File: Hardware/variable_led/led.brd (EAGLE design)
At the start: 160 x 100 mm, 12 parts

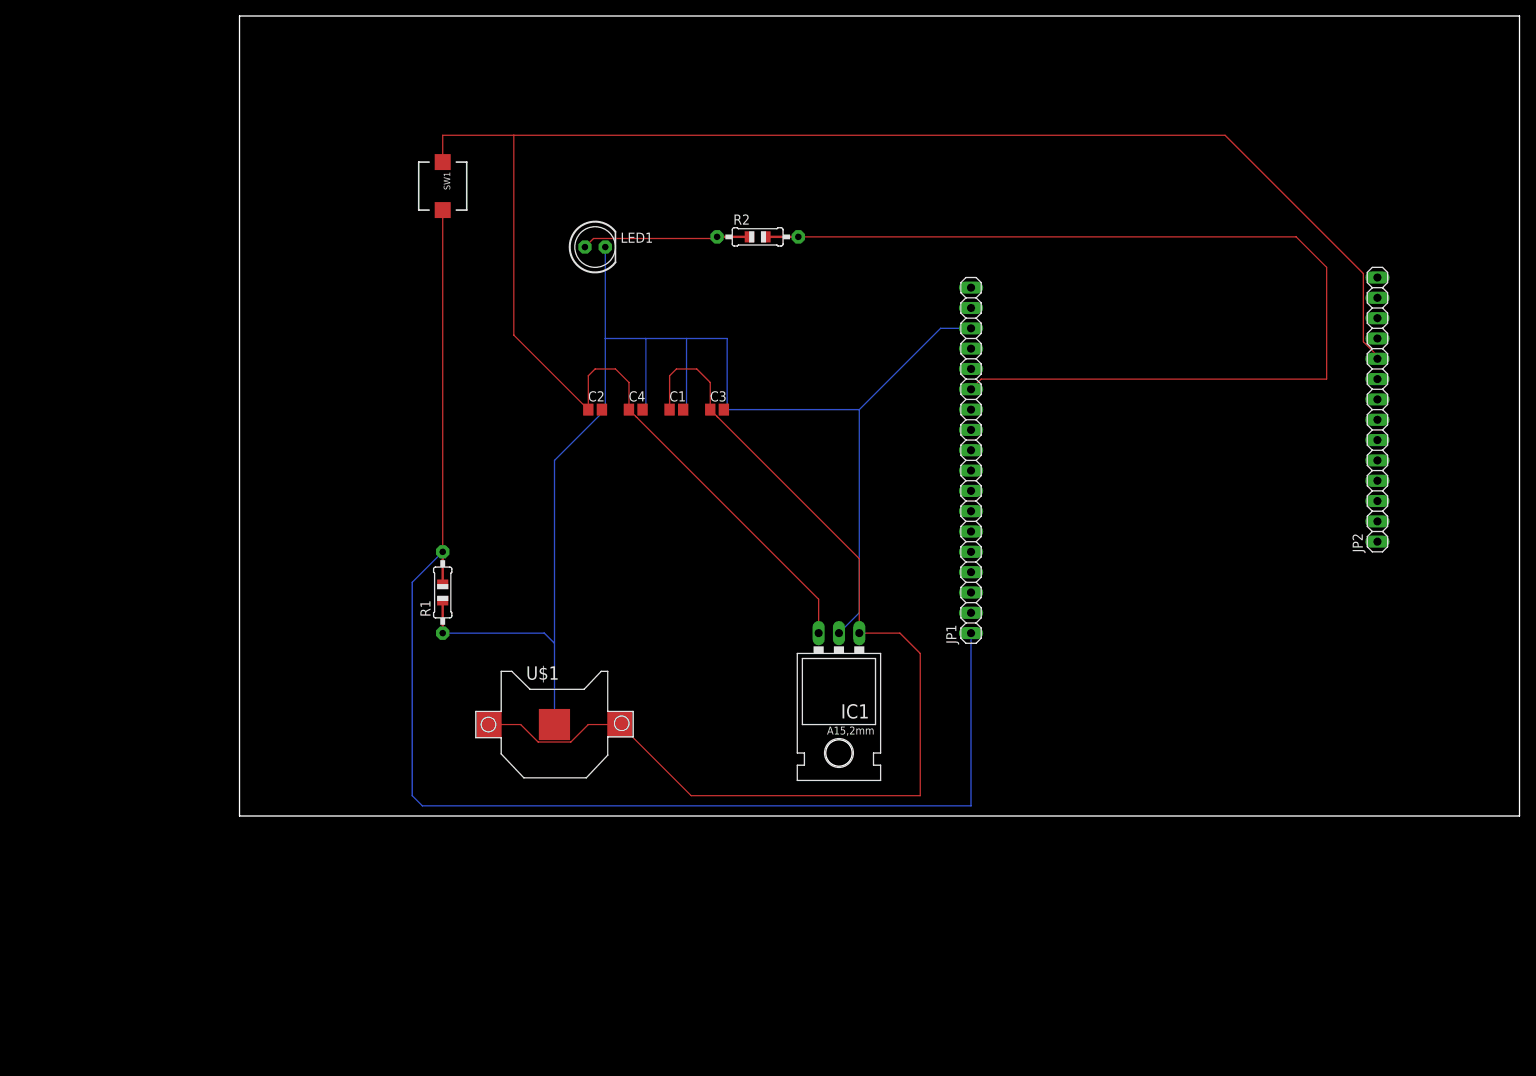
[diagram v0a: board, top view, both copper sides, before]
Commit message: Updated schematics without the voltage regulator
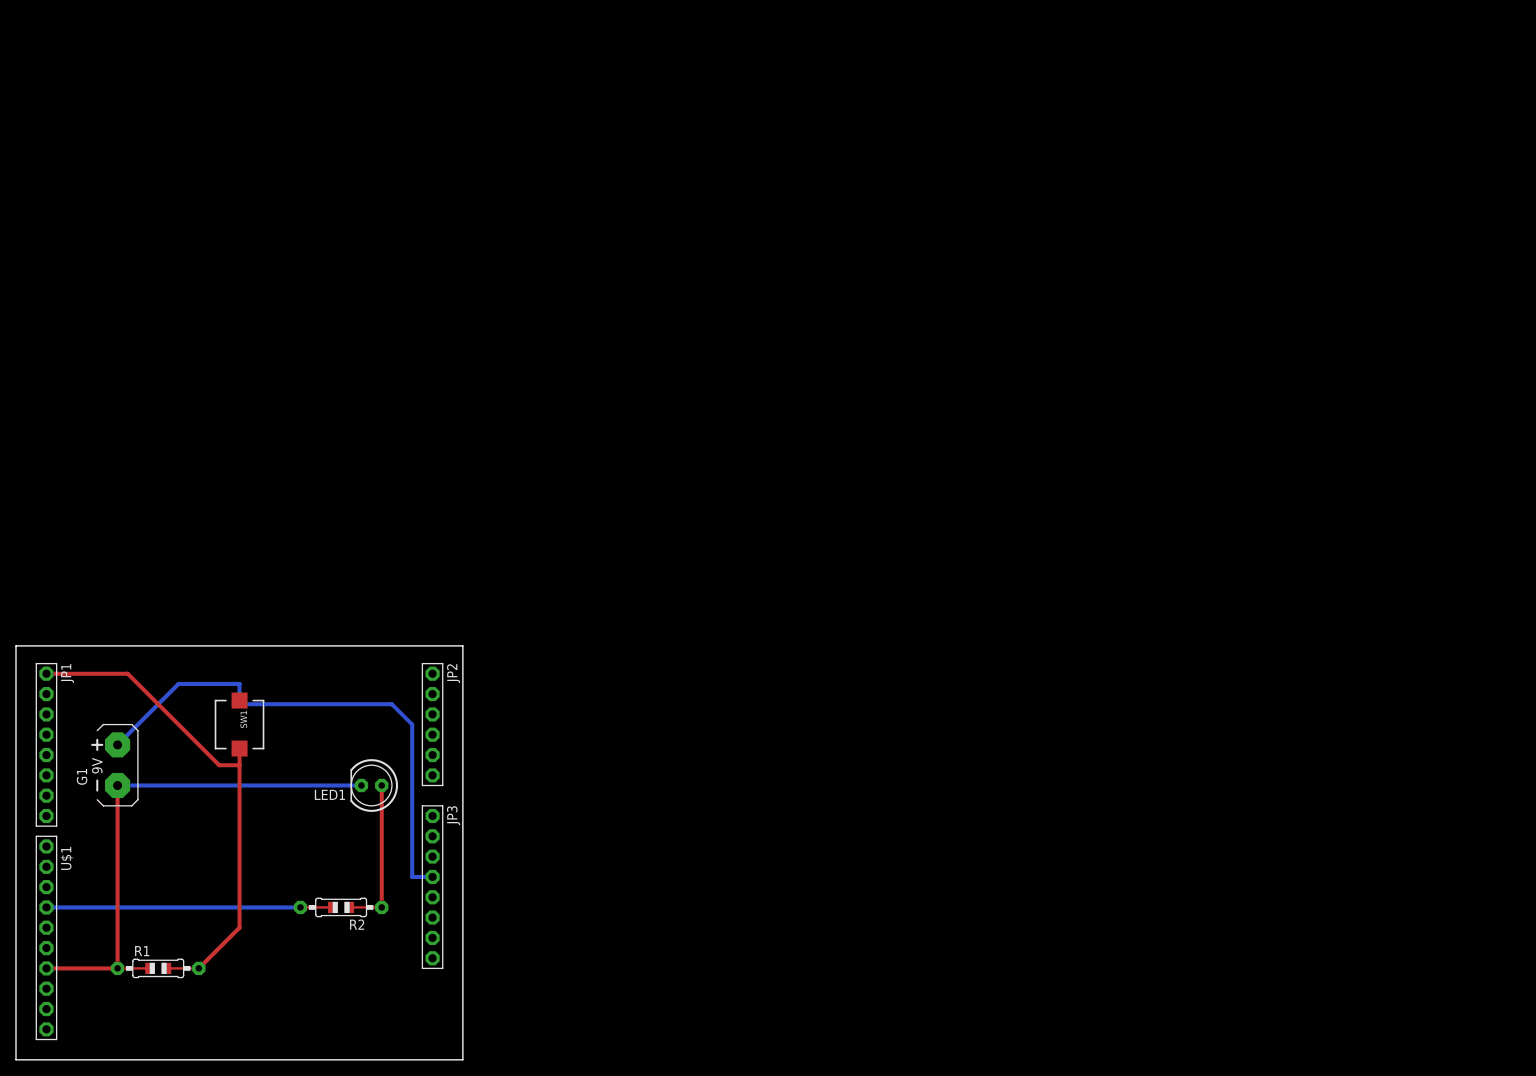
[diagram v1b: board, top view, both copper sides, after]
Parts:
- removed C1, C2: 10u, adafruit:C0805
- removed C3, C4: 0.1u, adafruit:C0805
- removed IC1: (no value), v-reg:78XXL
- added G1: AB9V, battery:AB9V
- added JP3: (no value), adafruit:1X08-BIG
- JP1: device adafruit:1X18 -> adafruit:1X08-BIG
- JP2: device adafruit:1X14 -> adafruit:1X06-BIG
- U$1: value 9V -> PINHD-1X10; device adafruit:CR1220-SMD -> adafruit:1X10-BIG
- moved JP2 124.5 mm to (24.1, 11.4), turned to 270 degrees
- moved JP1 120.9 mm to (-24.1, 8.89), turned to 270 degrees
- moved R2 98.7 mm to (12.7, -11.4), turned to 180 degrees
- moved LED1 72.9 mm to (16.5, 3.81), turned to 180 degrees
- moved SW1 71.9 mm to (0.00, 11.4)
- moved U$1 68.9 mm to (-24.1, -15.2), turned to 270 degrees
- moved R1 58.9 mm to (-10.2, -19.1), turned to 0 degrees
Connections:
- removed net V+: C1.1, C3.1, IC1.IN, U$1.+$1, U$1.+$2
- net 5V: now also G1.+, JP3.4; no longer C2.1, C4.1, IC1.OUT, JP2.10
- net GND: now also G1.-, U$1.7; no longer C1.2, C2.2, C3.2, C4.2, IC1.GND, JP1.16, U$1.-
- net N$2: now also U$1.4; no longer JP1.13
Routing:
- net 5V: track 228.3 -> 65.2 mm
- net V+: track 136.7 -> 0.00 mm
- net GND: track 182.4 -> 62.2 mm
- net N$4: track 166.9 -> 58.4 mm
- net N$2: track 126.6 -> 31.8 mm
- net N$3: track 17.0 -> 15.2 mm
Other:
- board size 160 x 100 mm -> 55.9 x 51.7 mm

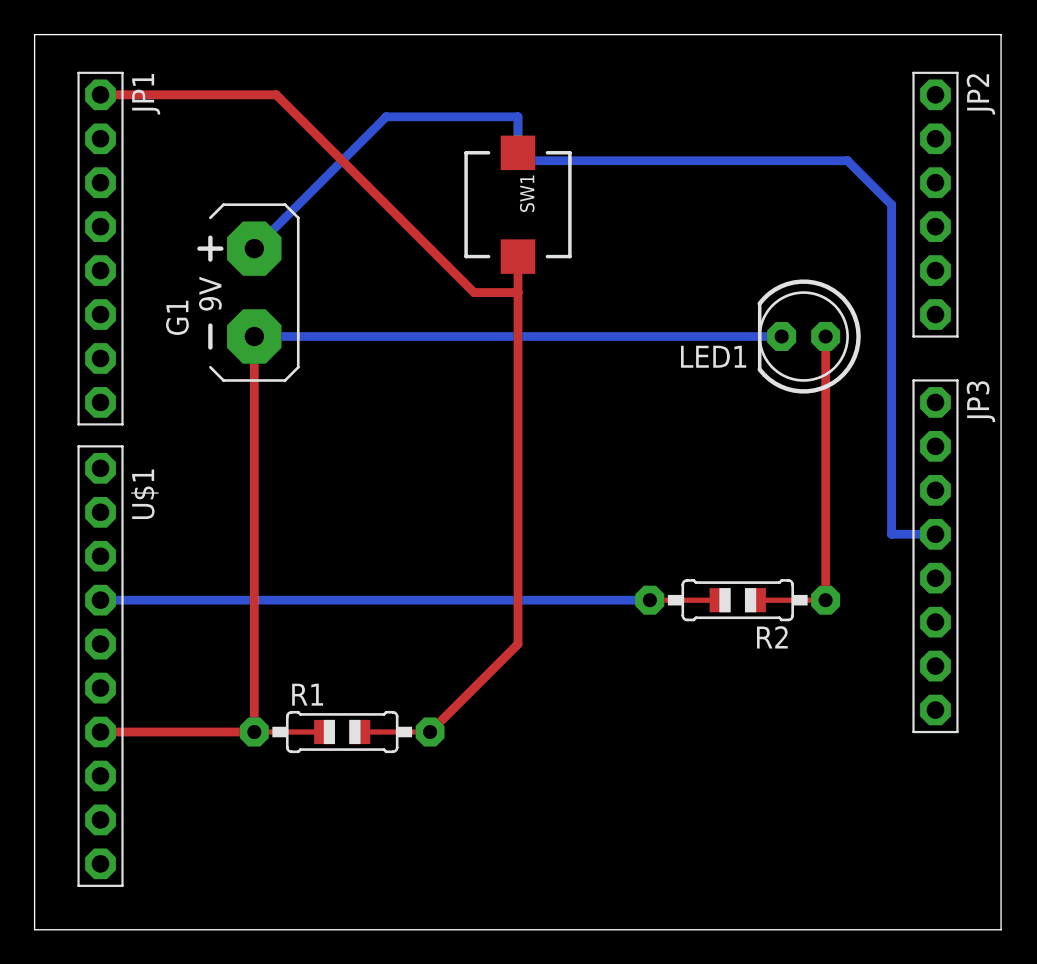
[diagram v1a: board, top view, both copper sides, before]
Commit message: Changed LED to two pins and changed board to single side
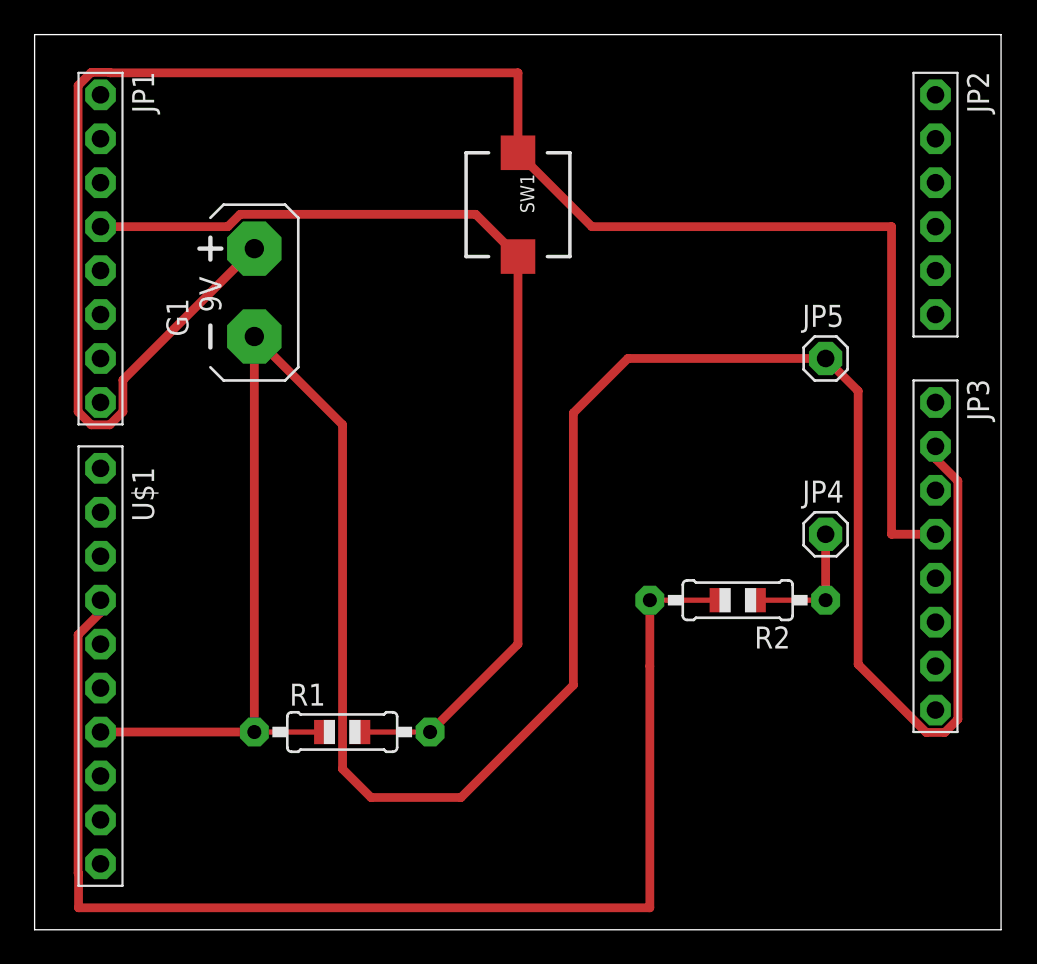
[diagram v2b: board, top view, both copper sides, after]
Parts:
- removed LED1: (no value), adafruit:LED5MM
- added JP4, JP5: (no value), adafruit:1X01
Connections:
- net GND: now also JP3.2, JP5.1; no longer LED1.K
- net N$3: now also JP4.1; no longer LED1.A
- net N$4: now also JP1.4; no longer JP1.1
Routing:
- net GND: track 62.2 -> 149.7 mm
- net 5V: track 65.2 -> 108.7 mm
- net N$2: track 31.8 -> 69.1 mm
- net N$3: track 15.2 -> 3.81 mm
- net N$4: track 58.4 -> 55.0 mm
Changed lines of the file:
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@@
 <dimension x1="24.13" y1="5.08" x2="24.13" y2="0" x3="29.21" y3="2.54" textsize="1.778" layer="1" unit="inch"/>
 <dimension x1="-24.13" y1="17.78" x2="24.13" y2="17.78" x3="0" y3="27.94" textsize="1.778" layer="1" unit="inch"/>
+<dimension x1="-27.94" y1="21.26" x2="27.92" y2="21.26" x3="-0.01" y3="31.75" textsize="1.778" layer="1" unit="inch"/>
+<dimension x1="-27.94" y1="21.26" x2="-27.94" y2="-30.48" x3="-36.83" y3="-4.61" textsize="1.778" layer="1" unit="inch"/>
 </plain>
 <attributes>
@@
 </autorouter>
 <elements>
-<element name="LED1" library="adafruit" library_urn="urn:adsk.eagle:library:420" package="LED5MM" package3d_urn="urn:adsk.eagle:package:6240538/1" value="" x="16.51" y="3.81" rot="R180">
-<attribute name="NAME" x="13.335" y="3.2766" size="1.27" layer="25" ratio="10" rot="R180"/>
-<attribute name="VALUE" x="13.3096" y="5.6134" size="1.27" layer="27" ratio="10" rot="R180"/>
-</element>
 <element name="R1" library="adafruit" library_urn="urn:adsk.eagle:library:420" package="0805-THM" package3d_urn="urn:adsk.eagle:package:6240726/1" value="100k" x="-10.16" y="-19.05">
 <attribute name="NAME" x="-13.208" y="-17.526" size="1.27" layer="25" ratio="10"/>
@@
 <attribute name="VALUE" x="20.955" y="1.27" size="1.27" layer="27" rot="R270"/>
 </element>
+<element name="JP4" library="adafruit" library_urn="urn:adsk.eagle:library:420" package="1X01" package3d_urn="urn:adsk.eagle:package:6240654/1" value="" x="17.78" y="-7.62">
+<attribute name="NAME" x="16.4338" y="-5.7912" size="1.27" layer="25" ratio="10"/>
+<attribute name="VALUE" x="16.51" y="-10.795" size="1.27" layer="27"/>
+</element>
+<element name="JP5" library="adafruit" library_urn="urn:adsk.eagle:library:420" package="1X01" package3d_urn="urn:adsk.eagle:package:6240654/1" value="" x="17.78" y="2.54">
+<attribute name="NAME" x="16.4338" y="4.3688" size="1.27" layer="25" ratio="10"/>
+<attribute name="VALUE" x="16.51" y="-0.635" size="1.27" layer="27"/>
+</element>
 </elements>
 <signals>
 <signal name="GND">
-<contactref element="LED1" pad="K"/>
 <contactref element="R1" pad="1"/>
 <contactref element="G1" pad="-"/>
@@
 <wire x1="-15.24" y1="3.81" x2="-15.24" y2="-19.05" width="0.508" layer="1"/>
 <wire x1="-15.24" y1="-19.05" x2="-24.13" y2="-19.05" width="0.508" layer="1"/>
-<wire x1="15.24" y1="3.81" x2="-15.24" y2="3.81" width="0.508" layer="16"/>
+<wire x1="-15.24" y1="3.81" x2="-10.141" y2="-1.289" width="0.508" layer="1"/>
+<wire x1="-10.141" y1="-1.289" x2="-10.141" y2="-21.1883375" width="0.508" layer="1"/>
+<wire x1="-8.4947375" y1="-22.8346" x2="-10.141" y2="-21.1883375" width="0.508" layer="1"/>
+<wire x1="-3.29446875" y1="-22.8346" x2="-8.4947375" y2="-22.8346" width="0.508" layer="1"/>
+<wire x1="3.2004" y1="-16.33973125" x2="-3.29446875" y2="-22.8346" width="0.508" layer="1"/>
+<contactref element="JP3" pad="2"/>
+<wire x1="23.593425" y1="-19.0754" x2="24.666575" y2="-19.0754" width="0.508" layer="1"/>
+<wire x1="24.666575" y1="-19.0754" x2="25.4254" y2="-18.316575" width="0.508" layer="1"/>
+<wire x1="25.4254" y1="-18.316575" x2="25.4254" y2="-4.543425" width="0.508" layer="1"/>
+<wire x1="19.6596" y1="-15.141575" x2="23.593425" y2="-19.0754" width="0.508" layer="1"/>
+<wire x1="24.13" y1="-3.248025" x2="24.13" y2="-2.54" width="0.508" layer="1"/>
+<wire x1="25.4254" y1="-4.543425" x2="24.13" y2="-3.248025" width="0.508" layer="1"/>
+<contactref element="JP5" pad="1"/>
+<wire x1="17.78" y1="2.54" x2="6.35" y2="2.54" width="0.508" layer="1"/>
+<wire x1="6.35" y1="2.54" x2="3.2004" y2="-0.6096" width="0.508" layer="1"/>
+<wire x1="3.2004" y1="-0.6096" x2="3.2004" y2="-16.33973125" width="0.508" layer="1"/>
+<wire x1="19.6596" y1="0.6604" x2="17.78" y2="2.54" width="0.508" layer="1"/>
+<wire x1="19.6596" y1="0.6604" x2="19.6596" y2="-15.141575" width="0.508" layer="1"/>
 </signal>
 <signal name="N$2">
 <contactref element="R2" pad="2"/>
 <contactref element="U$1" pad="4"/>
-<wire x1="7.62" y1="-11.43" x2="-24.13" y2="-11.43" width="0.508" layer="16"/>
+<wire x1="-24.13" y1="-11.43" x2="-24.13" y2="-12.138025" width="0.508" layer="1"/>
+<wire x1="-25.4254" y1="-27.206575" x2="-25.4" y2="-27.231975" width="0.508" layer="1"/>
+<wire x1="-25.4" y1="-27.231975" x2="-25.4" y2="-29.21" width="0.508" layer="1"/>
+<wire x1="-24.13" y1="-12.138025" x2="-25.4254" y2="-13.433425" width="0.508" layer="1"/>
+<wire x1="-25.4254" y1="-13.433425" x2="-25.4254" y2="-27.206575" width="0.508" layer="1"/>
+<wire x1="7.62" y1="-29.21" x2="-25.4" y2="-29.21" width="0.508" layer="1"/>
+<wire x1="7.62" y1="-11.43" x2="7.62" y2="-15.24" width="0.508" layer="1"/>
+<wire x1="7.62" y1="-15.24" x2="7.62" y2="-29.21" width="0.508" layer="1"/>
 </signal>
 <signal name="N$3">
 <contactref element="R2" pad="1"/>
-<contactref element="LED1" pad="A"/>
-<wire x1="17.78" y1="3.81" x2="17.78" y2="-11.43" width="0.508" layer="1"/>
+<contactref element="JP4" pad="1"/>
+<wire x1="17.78" y1="-7.62" x2="17.78" y2="-11.43" width="0.508" layer="1"/>
 </signal>
 <signal name="N$4">
 <contactref element="SW1" pad="P$1"/>
 <contactref element="R1" pad="2"/>
-<contactref element="JP1" pad="1"/>
-<wire x1="-13.97" y1="17.78" x2="-24.13" y2="17.78" width="0.508" layer="1"/>
-<wire x1="-2.54" y1="6.35" x2="-13.97" y2="17.78" width="0.508" layer="1"/>
-<wire x1="0" y1="6.35" x2="0" y2="-13.97" width="0.508" layer="1"/>
-<wire x1="0" y1="6.35" x2="-2.54" y2="6.35" width="0.508" layer="1"/>
+<wire x1="0" y1="8.43" x2="0" y2="-13.97" width="0.508" layer="1"/>
 <wire x1="0" y1="-13.97" x2="-5.08" y2="-19.05" width="0.508" layer="1"/>
-<wire x1="0" y1="8.43" x2="0" y2="6.35" width="0.508" layer="1"/>
+<contactref element="JP1" pad="4"/>
+<wire x1="-24.13" y1="10.16" x2="-16.77184375" y2="10.16" width="0.508" layer="1"/>
+<wire x1="-16.77184375" y1="10.16" x2="-16.06064375" y2="10.8712" width="0.508" layer="1"/>
+<wire x1="-16.06064375" y1="10.8712" x2="-2.4412" y2="10.8712" width="0.508" layer="1"/>
+<wire x1="-2.4412" y1="10.8712" x2="0" y2="8.43" width="0.508" layer="1"/>
 </signal>
 <signal name="5V">
@@
 <contactref element="G1" pad="+"/>
 <contactref element="JP3" pad="4"/>
-<wire x1="-7.62" y1="16.51" x2="-15.24" y2="8.89" width="0.508" layer="16"/>
-<wire x1="-7.62" y1="16.51" x2="0" y2="16.51" width="0.508" layer="16"/>
-<wire x1="21.59" y1="11.43" x2="21.59" y2="-7.62" width="0.508" layer="16"/>
-<wire x1="24.13" y1="-7.62" x2="21.59" y2="-7.62" width="0.508" layer="16"/>
-<wire x1="19.05" y1="13.97" x2="21.59" y2="11.43" width="0.508" layer="16"/>
-<wire x1="0" y1="16.51" x2="0" y2="13.97" width="0.508" layer="16"/>
-<wire x1="0" y1="13.97" x2="19.05" y2="13.97" width="0.508" layer="16"/>
-<wire x1="0" y1="13.97" x2="0" y2="14.43" width="0" layer="19" extent="1-16"/>
+<wire x1="-22.8346" y1="-0.536575" x2="-23.593425" y2="-1.2954" width="0.508" layer="1"/>
+<wire x1="-23.593425" y1="-1.2954" x2="-24.666575" y2="-1.2954" width="0.508" layer="1"/>
+<wire x1="-24.666575" y1="-1.2954" x2="-25.4254" y2="-0.536575" width="0.508" layer="1"/>
+<wire x1="-25.4254" y1="18.316575" x2="-24.666575" y2="19.0754" width="0.508" layer="1"/>
+<wire x1="-24.666575" y1="19.0754" x2="-23.593425" y2="19.0754" width="0.508" layer="1"/>
+<wire x1="-25.4254" y1="-0.536575" x2="-25.4254" y2="18.316575" width="0.508" layer="1"/>
+<wire x1="-15.24" y1="8.89" x2="-22.8346" y2="1.2954" width="0.508" layer="1"/>
+<wire x1="-22.8346" y1="1.2954" x2="-22.8346" y2="-0.536575" width="0.508" layer="1"/>
+<wire x1="-23.593425" y1="19.0754" x2="-23.568025" y2="19.05" width="0.508" layer="1"/>
+<wire x1="-23.568025" y1="19.05" x2="0" y2="19.05" width="0.508" layer="1"/>
+<wire x1="0" y1="19.05" x2="0" y2="14.43" width="0.508" layer="1"/>
+<wire x1="0" y1="14.43" x2="4.27" y2="10.16" width="0.508" layer="1"/>
+<wire x1="21.59" y1="10.16" x2="4.27" y2="10.16" width="0.508" layer="1"/>
+<wire x1="21.59" y1="10.16" x2="21.59" y2="-7.62" width="0.508" layer="1"/>
+<wire x1="21.59" y1="-7.62" x2="24.13" y2="-7.62" width="0.508" layer="1"/>
 </signal>
 </signals>
